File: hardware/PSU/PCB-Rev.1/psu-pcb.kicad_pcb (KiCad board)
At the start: 2 copper layers, 100 x 100 mm, 73 parts, among them J1 Conn_02x07_Odd_Even, J10 Conn_01x02, J11 Conn_01x02, J12 Conn_01x02, J13 Conn_01x02, J14 Conn_01x02, J15 Conn_01x02, J16 Conn_01x02, J2 OSTTC022162, J3 Conn_01x02, J4 Conn_01x02, J5 Conn_01x02, J6 Conn_01x02, J7 OSTTC022162, J8 Conn_01x05, J9 Conn_01x02, Q1 2N7000, Q2 2N7000, Q3 2N7000, Q4 FQP27P06, Q5 2N7000, U1 PIC12F1501-IP, U2 MCP3426-xSN

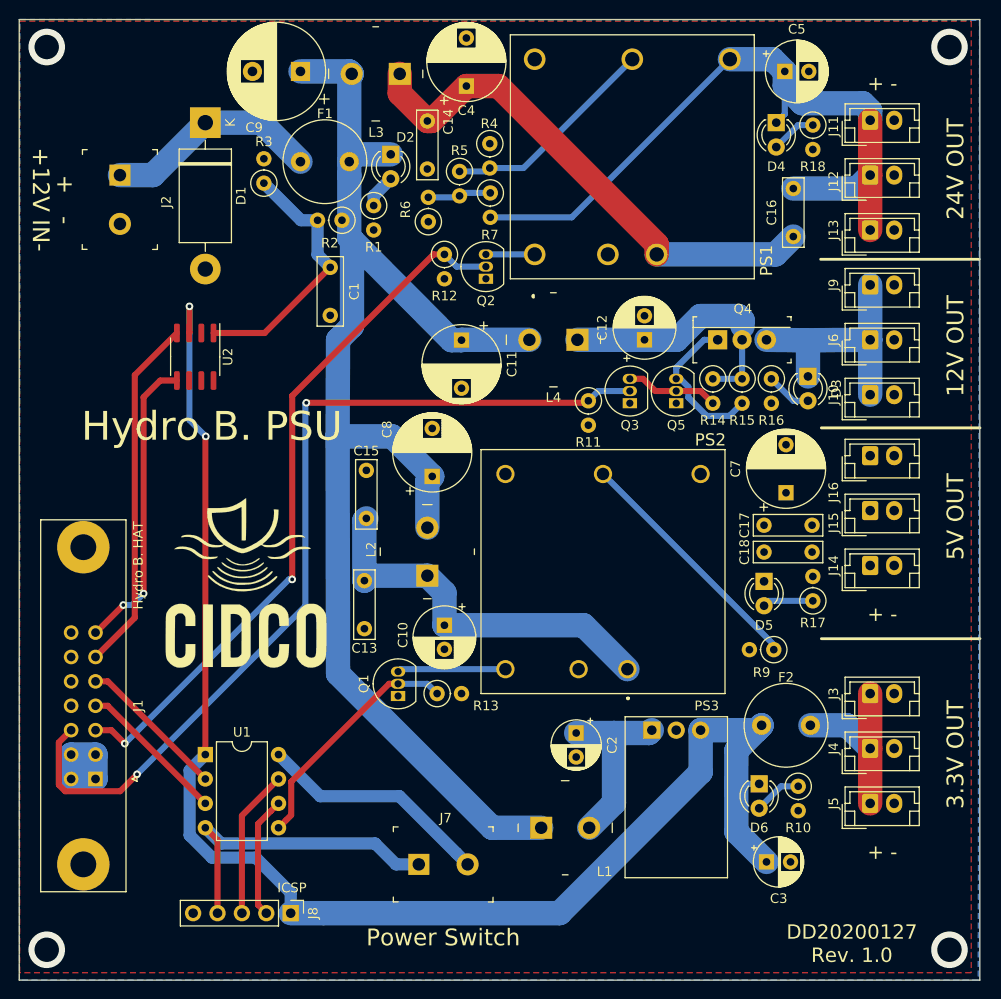
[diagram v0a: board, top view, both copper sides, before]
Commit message: mise a jours du fichier pcb pour l'alimentation pour que le rpi soit installer dessu avec des standoff pour permetre d'integrer le tout dans le catarob
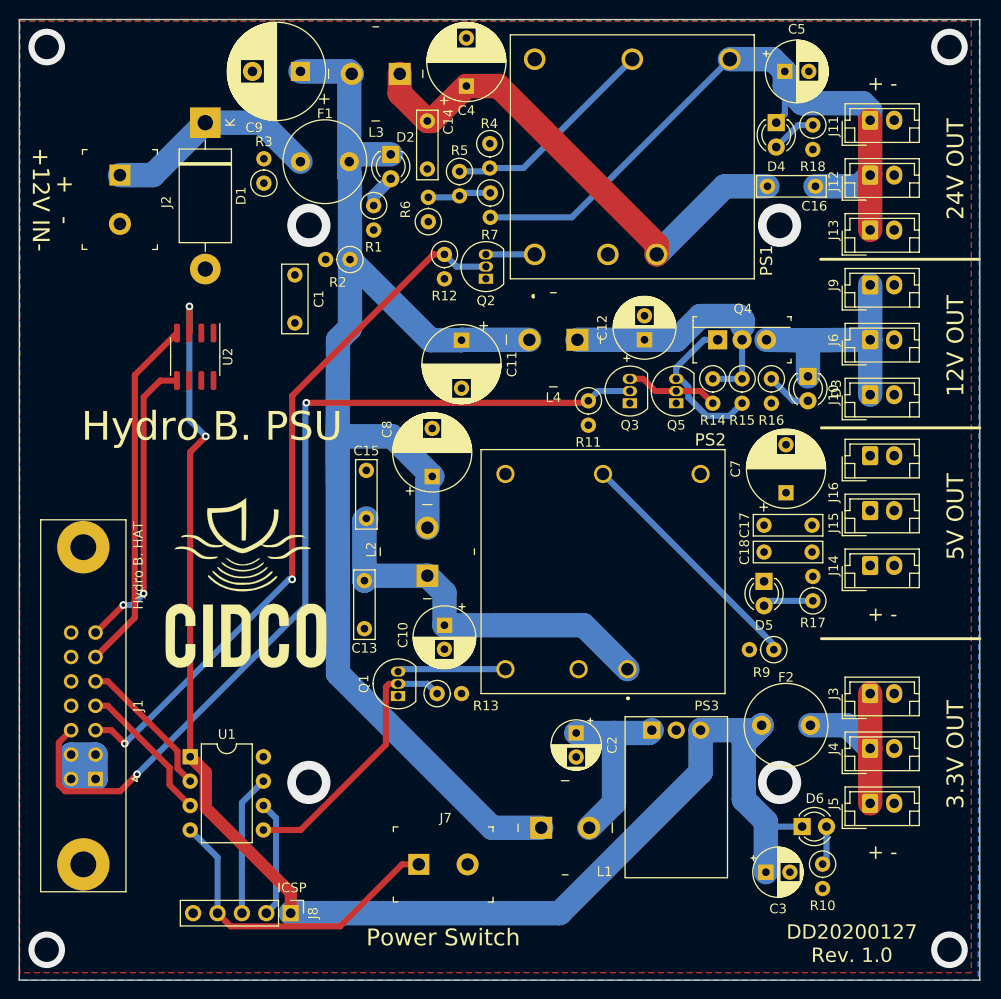
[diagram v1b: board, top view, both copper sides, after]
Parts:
- moved R10 8.49 mm to (103.6, 107.9)
- moved D6 6.30 mm to (101.5, 104.0), turned to 0 degrees
- moved C16 5.88 mm to (97.9, 37.4), turned to 0 degrees
- moved R2 4.17 mm to (54.4, 45.0)
- moved C1 3.77 mm to (48.7, 46.6)
- moved U1 1.59 mm to (37.8, 96.7)
- moved C3 1.07 mm to (97.7, 108.8)
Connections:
- C1 pad 1: Net-(C1-Pad1) -> (no net)
- R2 pad 2: Net-(C1-Pad1) -> (no net)
- R3 pad 1: Net-(C1-Pad1) -> (no net)
- U2 pad 1: Net-(C1-Pad1) -> (no net)
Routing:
- net Net-(C1-Pad1): track 27.6 -> 0.00 mm
- net GND: track 24.4 -> 0.00 mm, vias 4 -> 5
- net 5v_on: track 25.2 -> 28.3 mm
- net 24VOUT: track 76.2 -> 73.8 mm
- net (no net): track 0.00 -> 1.73 mm, vias 0 -> 3
- net +12V: track 141.3 -> 140.3 mm
- net Net-(D6-Pad2): track 5.01 -> 4.08 mm
- net ICSPDAT: track 15.5 -> 14.7 mm
- net read_sw: track 33.2 -> 34.0 mm
- net +3V3: track 153.1 -> 152.4 mm
- net Net-(C14-Pad1): track 54.5 -> 53.9 mm
- net ICSPCLK: track 12.7 -> 12.2 mm
